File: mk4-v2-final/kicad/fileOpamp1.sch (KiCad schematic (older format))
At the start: 7 parts, among them U2 LM358

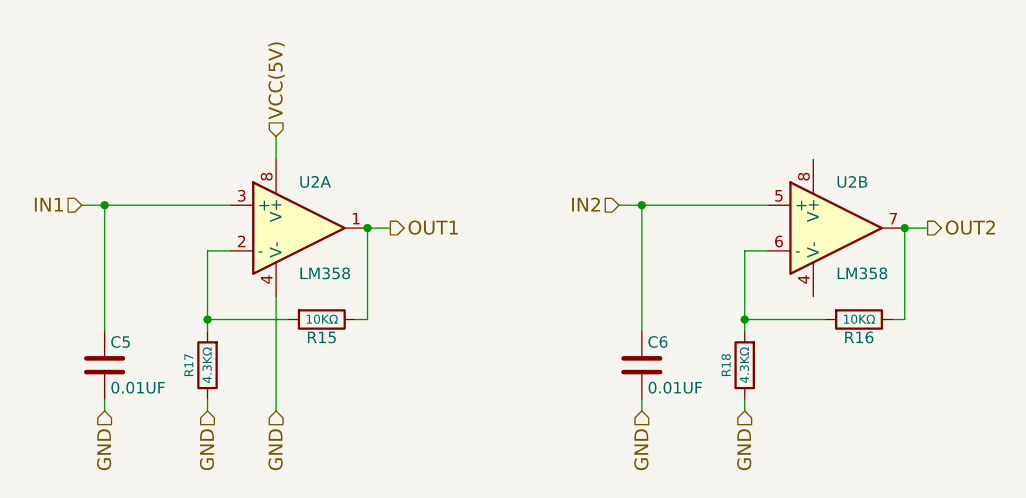
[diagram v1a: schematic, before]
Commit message: added headnight diodes, I don't think software control of them is going to be possible
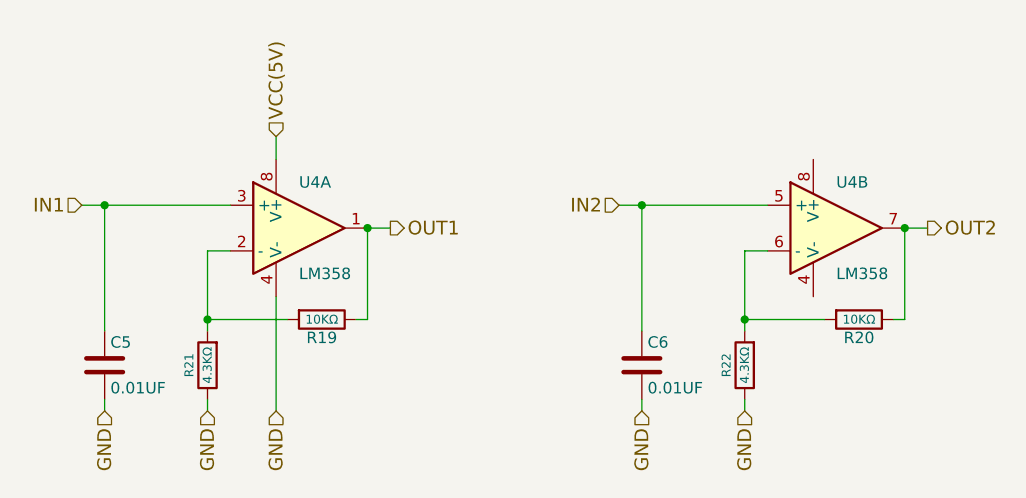
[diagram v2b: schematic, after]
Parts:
- renumbered R15 to R19, R16 to R20, R17 to R21, R18 to R22, U2 to U4
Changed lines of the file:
@@
 $EndDescr
 $Comp
-L LM358 U2
+L LM358 U4
 U 1 1 59DEDBFA
 P 4950 3850
-F 0 "U2" H 4950 4050 50  0000 L CNN
+F 0 "U4" H 4950 4050 50  0000 L CNN
 F 1 "LM358" H 4950 3650 50  0000 L CNN
 F 2 "Housings_DIP:DIP-8_W7.62mm" H 4950 3850 50  0001 C CNN
@@
 $EndComp
 $Comp
-L LM358 U2
+L LM358 U4
 U 2 1 59DEDC01
 P 7300 3850
-F 0 "U2" H 7300 4050 50  0000 L CNN
+F 0 "U4" H 7300 4050 50  0000 L CNN
 F 1 "LM358" H 7300 3650 50  0000 L CNN
 F 2 "Housings_DIP:DIP-8_W7.62mm" H 7300 3850 50  0001 C CNN
@@
 $EndComp
 $Comp
-L R R15
+L R R19
 U 1 1 59DEDC0E
 P 5050 4250
-F 0 "R15" V 5130 4250 50  0000 C CNN
+F 0 "R19" V 5130 4250 50  0000 C CNN
 F 1 "10KΩ" V 5050 4250 39  0000 C CNN
 F 2 "Resistors_THT:R_Axial_DIN0207_L6.3mm_D2.5mm_P10.16mm_Horizontal" V 4980 4250 50  0001 C CNN
@@
 $EndComp
 $Comp
-L R R17
+L R R21
 U 1 1 59DEDC15
 P 4550 4450
-F 0 "R17" V 4630 4450 39  0000 C CNN
+F 0 "R21" V 4630 4450 39  0000 C CNN
 F 1 "4.3KΩ" V 4550 4450 39  0000 C CNN
 F 2 "Resistors_THT:R_Axial_DIN0207_L6.3mm_D2.5mm_P10.16mm_Horizontal" V 4480 4450 50  0001 C CNN
@@
 $EndComp
 $Comp
-L R R16
+L R R20
 U 1 1 59DEDC22
 P 7400 4250
-F 0 "R16" V 7480 4250 50  0000 C CNN
+F 0 "R20" V 7480 4250 50  0000 C CNN
 F 1 "10KΩ" V 7400 4250 39  0000 C CNN
 F 2 "Resistors_THT:R_Axial_DIN0207_L6.3mm_D2.5mm_P10.16mm_Horizontal" V 7330 4250 50  0001 C CNN
@@
 IN2
 $Comp
-L R R18
+L R R22
 U 1 1 59DEDC45
 P 6900 4450
-F 0 "R18" V 6980 4450 39  0000 C CNN
+F 0 "R22" V 6980 4450 39  0000 C CNN
 F 1 "4.3KΩ" V 6900 4450 39  0000 C CNN
 F 2 "Resistors_THT:R_Axial_DIN0207_L6.3mm_D2.5mm_P10.16mm_Horizontal" V 6830 4450 50  0001 C CNN

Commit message: schematic is done, footprint association and netlist are also done
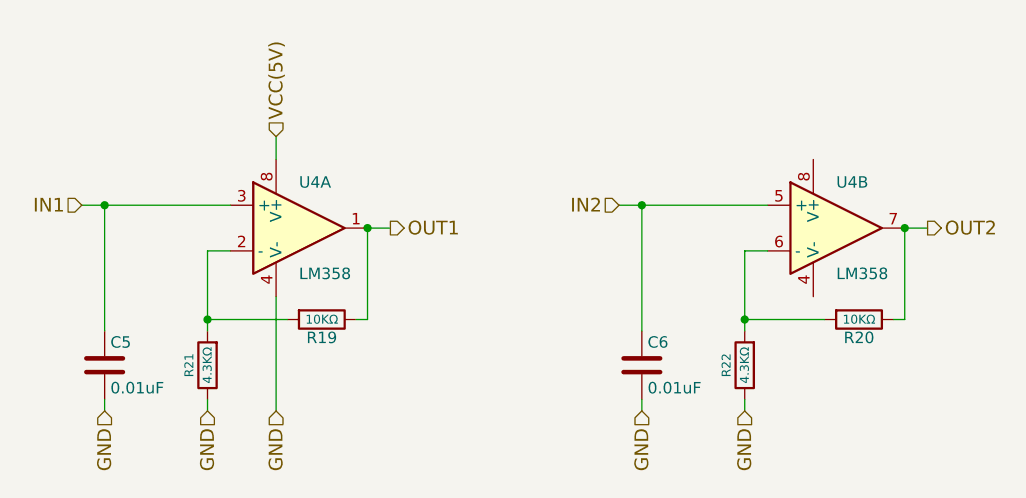
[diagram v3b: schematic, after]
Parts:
- C5, C6: value 0.01UF -> 0.01uF; footprint Capacitors_THT:C_Disc_D12.0mm_W4.4mm_P7.75mm -> C_Rect_L5.08mm_W3.175mm_P2.54mm:C_Rect_L5.08mm_W3.175mm_P2.54mm; digikey-pn (none) -> 478-5095-ND; mfg-pn (none) -> AR205F103K4R
- R19, R20: footprint Resistors_THT:R_Axial_DIN0207_L6.3mm_D2.5mm_P10.16mm_Horizontal -> Resistors_THT:R_Axial_DIN0204_L3.6mm_D1.6mm_P5.08mm_Horizontal; digikey-pn (none) -> BC10.0KXCT-ND; mfg-pn (none) -> MBA02040C1002FRP00
- R21, R22: footprint Resistors_THT:R_Axial_DIN0207_L6.3mm_D2.5mm_P10.16mm_Horizontal -> Resistors_THT:R_Axial_DIN0204_L3.6mm_D1.6mm_P5.08mm_Horizontal; digikey-pn (none) -> BC3513CT-ND; mfg-pn (none) -> MBA02040C4301FC100
- U4: digikey-pn (none) -> 296-1395-5-ND; mfg-pn (none) -> LM358P
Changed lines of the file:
@@
 EESchema Schematic File Version 2
-LIBS:hitchco-mk4-rescue
 LIBS:power
 LIBS:device
@@
 LIBS:cd4013b
 LIBS:ncs3s1205sc
+LIBS:lca715
+LIBS:SN74HC595N
+LIBS:CD74HC4067
 LIBS:hitchco-mk4-cache
 EELAYER 25 0
@@
 F 2 "Housings_DIP:DIP-8_W7.62mm" H 4950 3850 50  0001 C CNN
 F 3 "http://www.ti.com/lit/ds/symlink/lm358.pdf" H 4950 3850 50  0001 C CNN
+F 4 "296-1395-5-ND" H 4950 4150 50  0001 C CNN "digikey-pn"
+F 5 "LM358P" H 4950 4150 50  0001 C CNN "mfg-pn"
 	1    4950 3850
 	1    0    0    -1
@@
 F 1 "LM358" H 7300 3650 50  0000 L CNN
 F 2 "Housings_DIP:DIP-8_W7.62mm" H 7300 3850 50  0001 C CNN
-F 3 "" H 7300 3850 50  0001 C CNN
+F 3 "http://www.ti.com/lit/ds/symlink/lm358.pdf" H 7300 3850 50  0001 C CNN
+F 4 "296-1395-5-ND" H 7300 4150 50  0001 C CNN "digikey-pn"
+F 5 "LM358P" H 7300 4150 50  0001 C CNN "mfg-pn"
 	2    7300 3850
 	1    0    0    -1
@@
 F 0 "R19" V 5130 4250 50  0000 C CNN
 F 1 "10KΩ" V 5050 4250 39  0000 C CNN
-F 2 "Resistors_THT:R_Axial_DIN0207_L6.3mm_D2.5mm_P10.16mm_Horizontal" V 4980 4250 50  0001 C CNN
+F 2 "Resistors_THT:R_Axial_DIN0204_L3.6mm_D1.6mm_P5.08mm_Horizontal" V 4980 4250 50  0001 C CNN
 F 3 "" H 5050 4250 50  0001 C CNN
+F 4 "BC10.0KXCT-ND" H 5130 4350 50  0001 C CNN "digikey-pn"
+F 5 "MBA02040C1002FRP00" H 5130 4350 50  0001 C CNN "mfg-pn"
 	1    5050 4250
 	0    1    1    0
@@
 F 0 "R21" V 4630 4450 39  0000 C CNN
 F 1 "4.3KΩ" V 4550 4450 39  0000 C CNN
-F 2 "Resistors_THT:R_Axial_DIN0207_L6.3mm_D2.5mm_P10.16mm_Horizontal" V 4480 4450 50  0001 C CNN
+F 2 "Resistors_THT:R_Axial_DIN0204_L3.6mm_D1.6mm_P5.08mm_Horizontal" V 4480 4450 50  0001 C CNN
 F 3 "" H 4550 4450 50  0001 C CNN
+F 4 "BC3513CT-ND" H 4630 4550 50  0001 C CNN "digikey-pn"
+F 5 "MBA02040C4301FC100" H 4630 4550 50  0001 C CNN "mfg-pn"
 	1    4550 4450
 	-1   0    0    1
@@
 F 0 "R20" V 7480 4250 50  0000 C CNN
 F 1 "10KΩ" V 7400 4250 39  0000 C CNN
-F 2 "Resistors_THT:R_Axial_DIN0207_L6.3mm_D2.5mm_P10.16mm_Horizontal" V 7330 4250 50  0001 C CNN
+F 2 "Resistors_THT:R_Axial_DIN0204_L3.6mm_D1.6mm_P5.08mm_Horizontal" V 7330 4250 50  0001 C CNN
 F 3 "" H 7400 4250 50  0001 C CNN
+F 4 "BC10.0KXCT-ND" H 7480 4350 50  0001 C CNN "digikey-pn"
+F 5 "MBA02040C1002FRP00" H 7480 4350 50  0001 C CNN "mfg-pn"
 	1    7400 4250
 	0    1    1    0
+$EndComp
+$Comp
+L R R22
+U 1 1 59DEDC45
+P 6900 4450
+F 0 "R22" V 6980 4450 39  0000 C CNN
+F 1 "4.3KΩ" V 6900 4450 39  0000 C CNN
+F 2 "Resistors_THT:R_Axial_DIN0204_L3.6mm_D1.6mm_P5.08mm_Horizontal" V 6830 4450 50  0001 C CNN
+F 3 "" H 6900 4450 50  0001 C CNN
+F 4 "BC3513CT-ND" H 6980 4550 50  0001 C CNN "digikey-pn"
+F 5 "MBA02040C4301FC100" H 6980 4550 50  0001 C CNN "mfg-pn"
+	1    6900 4450
+	-1   0    0    1
+$EndComp
+$Comp
+L C C5
+U 1 1 59DEDC4C
+P 4100 4450
+F 0 "C5" H 4125 4550 50  0000 L CNN
+F 1 "0.01uF" H 4125 4350 50  0000 L CNN
+F 2 "C_Rect_L5.08mm_W3.175mm_P2.54mm:C_Rect_L5.08mm_W3.175mm_P2.54mm" H 4138 4300 50  0001 C CNN
+F 3 "http://datasheets.avx.com/AR-Series.pdf" H 4100 4450 50  0001 C CNN
+F 4 "478-5095-ND" H 4125 4650 50  0001 C CNN "digikey-pn"
+F 5 "AR205F103K4R" H 4125 4650 50  0001 C CNN "mfg-pn"
+	1    4100 4450
+	1    0    0    -1
+$EndComp
+$Comp
+L C C6
+U 1 1 5A20E4CC
+P 6450 4450
+F 0 "C6" H 6475 4550 50  0000 L CNN
+F 1 "0.01uF" H 6475 4350 50  0000 L CNN
+F 2 "C_Rect_L5.08mm_W3.175mm_P2.54mm:C_Rect_L5.08mm_W3.175mm_P2.54mm" H 6488 4300 50  0001 C CNN
+F 3 "http://datasheets.avx.com/AR-Series.pdf" H 6450 4450 50  0001 C CNN
+F 4 "478-5095-ND" H 6475 4650 50  0001 C CNN "digikey-pn"
+F 5 "AR205F103K4R" H 6475 4650 50  0001 C CNN "mfg-pn"
+	1    6450 4450
+	1    0    0    -1
 $EndComp
 Text HLabel 5350 3850 2    60   Output ~ 0
@@
 Text HLabel 6350 3750 0    60   Input ~ 0
 IN2
-$Comp
-L R R22
-U 1 1 59DEDC45
-P 6900 4450
-F 0 "R22" V 6980 4450 39  0000 C CNN
-F 1 "4.3KΩ" V 6900 4450 39  0000 C CNN
-F 2 "Resistors_THT:R_Axial_DIN0207_L6.3mm_D2.5mm_P10.16mm_Horizontal" V 6830 4450 50  0001 C CNN
-F 3 "" H 6900 4450 50  0001 C CNN
-	1    6900 4450
-	-1   0    0    1
-$EndComp
-$Comp
-L C C5
-U 1 1 59DEDC4C
-P 4100 4450
-F 0 "C5" H 4125 4550 50  0000 L CNN
-F 1 "0.01UF" H 4125 4350 50  0000 L CNN
-F 2 "Capacitors_THT:C_Disc_D12.0mm_W4.4mm_P7.75mm" H 4138 4300 50  0001 C CNN
-F 3 "http://www.vishay.com/docs/28515/sseries.pdf" H 4100 4450 50  0001 C CNN
-	1    4100 4450
-	1    0    0    -1
-$EndComp
+Text HLabel 4100 4650 3    60   Input ~ 0
+GND
+Text HLabel 4550 4650 3    60   Input ~ 0
+GND
+Text HLabel 4850 4650 3    60   Input ~ 0
+GND
+Text HLabel 6450 4650 3    60   Input ~ 0
+GND
+Text HLabel 6900 4650 3    60   Input ~ 0
+GND
+Text HLabel 4850 3450 1    60   Input ~ 0
+VCC(5V)
 Wire Wire Line
 	4550 4250 4900 4250
@@
 Wire Wire Line
 	4650 3950 4550 3950
+Wire Wire Line
+	4550 3950 4550 4300
+Wire Wire Line
+	4550 4650 4550 4600
+Wire Wire Line
+	7550 4250 7600 4250
+Wire Wire Line
+	7600 4250 7600 3850
+Wire Wire Line
+	6900 4650 6900 4600
+Wire Wire Line
+	6900 3950 6900 4300
+Wire Wire Line
+	6900 4250 7250 4250
+Wire Wire Line
+	6900 3950 7000 3950
+Wire Wire Line
+	4850 4650 4850 4150
+Wire Wire Line
+	4850 3550 4850 3450
+Wire Wire Line
+	5250 3850 5350 3850
+Wire Wire Line
+	7600 3850 7700 3850
+Wire Wire Line
+	4000 3750 4650 3750
+Wire Wire Line
+	4100 4300 4100 3750
+Wire Wire Line
+	6450 4300 6450 3750
+Wire Wire Line
+	6350 3750 7000 3750
+Wire Wire Line
+	4100 4600 4100 4650
+Wire Wire Line
+	6450 4650 6450 4600
+Wire Wire Line
+	5250 3850 5250 4250
 Connection ~ 4550 4250
-Wire Wire Line
-	4550 3950 4550 4300
-Wire Wire Line
-	4550 4650 4550 4600
-Wire Wire Line
-	7550 4250 7600 4250
-Wire Wire Line
-	7600 4250 7600 3850
-Wire Wire Line
-	6900 4650 6900 4600
-Wire Wire Line
-	6900 3950 6900 4300
-Wire Wire Line
-	6900 4250 7250 4250
 Connection ~ 6900 4250
-Wire Wire Line
-	6900 3950 7000 3950
-Wire Wire Line
-	4850 4650 4850 4150
-Wire Wire Line
-	4850 3550 4850 3450
-Wire Wire Line
-	5250 3850 5350 3850
 Connection ~ 5250 3850
 Connection ~ 7600 3850
-Wire Wire Line
-	7600 3850 7700 3850
-Wire Wire Line
-	4000 3750 4650 3750
-Wire Wire Line
-	4100 4300 4100 3750
-Wire Wire Line
-	6450 4300 6450 3750
-Wire Wire Line
-	6350 3750 7000 3750
-Wire Wire Line
-	4100 4600 4100 4650
-Wire Wire Line
-	6450 4650 6450 4600
-Text HLabel 4100 4650 3    60   Input ~ 0
-GND
-Text HLabel 4550 4650 3    60   Input ~ 0
-GND
-Text HLabel 4850 4650 3    60   Input ~ 0
-GND
-Text HLabel 6450 4650 3    60   Input ~ 0
-GND
-Text HLabel 6900 4650 3    60   Input ~ 0
-GND
-Text HLabel 4850 3450 1    60   Input ~ 0
-VCC(5V)
 Connection ~ 4100 3750
 Connection ~ 6450 3750
-$Comp
-L C C6
-U 1 1 5A20E4CC
-P 6450 4450
-F 0 "C6" H 6475 4550 50  0000 L CNN
-F 1 "0.01UF" H 6475 4350 50  0000 L CNN
-F 2 "Capacitors_THT:C_Disc_D12.0mm_W4.4mm_P7.75mm" H 6488 4300 50  0001 C CNN
-F 3 "http://www.vishay.com/docs/28515/sseries.pdf" H 6450 4450 50  0001 C CNN
-	1    6450 4450
-	1    0    0    -1
-$EndComp
-Wire Wire Line
-	5250 3850 5250 4250
 $EndSCHEMATC
